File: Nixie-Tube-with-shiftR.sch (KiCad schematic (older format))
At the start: 56 parts, among them J1 Conn_01x06_Male, J2 HV_IN, J3 Conn_01x06_Female, J4 HV_OUT, Q1 MMBTA42LT1, Q10 MMBTA42LT1, Q11 AO3400, Q12 AO3400, Q13 AO3400, Q14 MMBTA42LT1, Q15 MMBTA42LT1, Q2 MMBTA42LT1, Q3 MMBTA42LT1, Q4 MMBTA42LT1, Q5 MMBTA42LT1, Q6 MMBTA42LT1, Q7 MMBTA42LT1, Q8 MMBTA42LT1, Q9 MMBTA42LT1, U1 74HC595D, U2 nixie-tube, U3 74HC595D, U4 ams1117-5.0

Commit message: rename file according to the project
nixie-tube-display-with-shiftR is qs27 while roundxx is qs30
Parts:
- removed U2: nixie-tube, symbol nixie-tube
- added U?: nixie-tube-qs27, symbol nixie-tube-qs27
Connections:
- no-connect marks 3 -> 1
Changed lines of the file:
@@
 $EndComp
 $Comp
-L nixie-tube U2
-U 1 1 5A0CB7BC
+L nixie-tube-qs27 U?
+U 1 1 5A0CF6F4
 P 5450 1950
-F 0 "U2" H 4875 2050 60  0000 C CNN
-F 1 "nixie-tube" H 5625 2275 60  0000 C CNN
+F 0 "U?" H 4875 2050 60  0000 C CNN
+F 1 "nixie-tube-qs27" H 5625 2275 60  0000 C CNN
 F 2 "" H 5150 1975 60  0001 C CNN
 F 3 "" H 5150 1975 60  0001 C CNN
@@
 	1    0    0    -1
 $EndComp
-NoConn ~ 5025 1325
-NoConn ~ 5150 1325
 $EndSCHEMATC

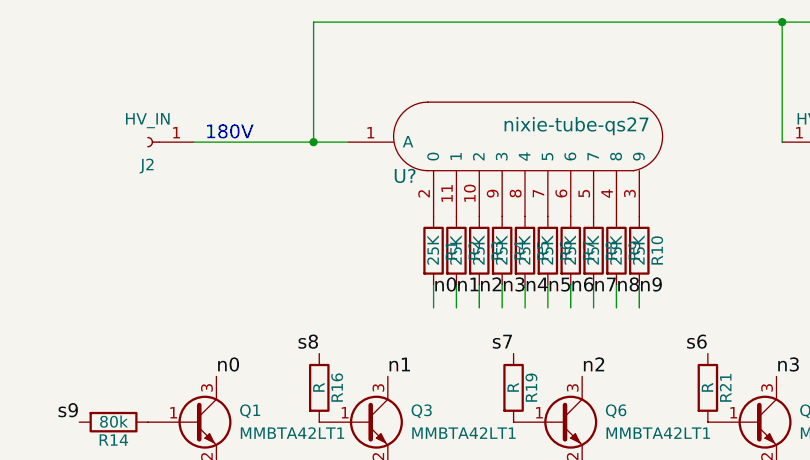
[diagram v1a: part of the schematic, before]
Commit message: remove silkscreen on female pins, re routed some of the tracks
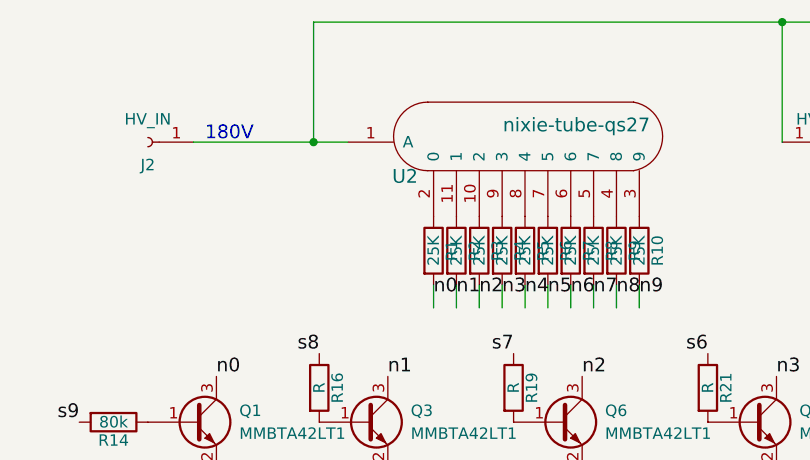
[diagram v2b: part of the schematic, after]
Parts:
- J2: footprint Socket_Strips:Socket_Strip_Angled_1x01_Pitch2.54mm -> nixie-tube-fp:Socket_Strip_Angled_1x01_Pitch2.54mm_without_silk
- J3: footprint Socket_Strips:Socket_Strip_Angled_1x06_Pitch2.54mm -> nixie-tube-fp:Socket_Strip_Angled_1x06_Pitch2.54mm_without_silk
- gave numbers to parts that had none: 1
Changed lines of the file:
@@
 F 0 "J2" H 3750 1800 50  0000 C CNN
 F 1 "HV_IN" H 3750 1600 50  0000 C CNN
-F 2 "Socket_Strips:Socket_Strip_Angled_1x01_Pitch2.54mm" H 3750 1700 50  0001 C CNN
+F 2 "nixie-tube-fp:Socket_Strip_Angled_1x01_Pitch2.54mm_without_silk" H 3750 1700 50  0001 C CNN
 F 3 "" H 3750 1700 50  0001 C CNN
 	1    3750 1700
@@
 F 0 "J3" H 3525 4150 50  0000 C CNN
 F 1 "Conn_01x06_Female" H 3525 3450 50  0000 C CNN
-F 2 "Socket_Strips:Socket_Strip_Angled_1x06_Pitch2.54mm" H 3525 3850 50  0001 C CNN
+F 2 "nixie-tube-fp:Socket_Strip_Angled_1x06_Pitch2.54mm_without_silk" H 3525 3850 50  0001 C CNN
 F 3 "" H 3525 3850 50  0001 C CNN
 	1    3525 3850
@@
 $EndComp
 $Comp
-L nixie-tube-qs27 U?
+L nixie-tube-qs27 U2
 U 1 1 5A0CF6F4
 P 5450 1950
-F 0 "U?" H 4875 2050 60  0000 C CNN
+F 0 "U2" H 4875 2050 60  0000 C CNN
 F 1 "nixie-tube-qs27" H 5625 2275 60  0000 C CNN
 F 2 "" H 5150 1975 60  0001 C CNN

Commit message: fixed various bugs
RGB led not connected properly to the mosfet
AO3400 pin orientation is not same with datasheet
move silkscreen away on neon footprint
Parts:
- removed D1: LED_CRGB, nixie-tube-fp:Rgb-Led, symbol LED_CRGB
- removed Q11, Q12, Q13: AO3400, TO_SOT_Packages_SMD:SOT-23, symbol 2N7000
- added D1: LED_RGB_BGR, nixie-tube-fp:LED_RGB_5050-6, symbol LED_RGB_BGR
- added Q11, Q12, Q13: AO3400, TO_SOT_Packages_SMD:SOT-23, symbol 2N7002
- U2: footprint (none) -> nixie-tube-fp:qs27-1
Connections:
- wire segments 66 -> 68
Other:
- moved on the sheet: R11, R12, R13
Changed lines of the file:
@@
 	6525 5700 6525 5725
 NoConn ~ 6325 4250
-$Comp
-L LED_CRGB D1
-U 1 1 59DF14B9
-P 8375 5750
-F 0 "D1" H 8375 6120 50  0000 C CNN
-F 1 "LED_CRGB" H 8375 5400 50  0000 C CNN
-F 2 "nixie-tube-fp:Rgb-Led" H 8375 5700 50  0001 C CNN
-F 3 "" H 8375 5700 50  0001 C CNN
-	1    8375 5750
-	0    -1   -1   0
-$EndComp
-$Comp
-L GND #PWR05
-U 1 1 59DF166A
-P 8375 5950
-F 0 "#PWR05" H 8375 5700 50  0001 C CNN
-F 1 "GND" H 8375 5800 50  0000 C CNN
-F 2 "" H 8375 5950 50  0001 C CNN
-F 3 "" H 8375 5950 50  0001 C CNN
-	1    8375 5950
-	1    0    0    -1
-$EndComp
 Text Label 7725 5150 2    60   ~ 0
 Red
-Text Label 8625 5175 2    60   ~ 0
+Text Label 8625 5150 2    60   ~ 0
 Green
-Text Label 9400 5175 2    60   ~ 0
+Text Label 9400 5150 2    60   ~ 0
 Blue
 Text Label 5825 4250 1    60   ~ 0
@@
 Blue
 Wire Wire Line
-	8025 5350 8025 5550
-Wire Wire Line
-	8025 5550 8175 5550
-Wire Wire Line
-	8925 5375 8375 5375
-Wire Wire Line
-	8375 5375 8375 5550
-Wire Wire Line
-	9700 5375 9700 5550
-Wire Wire Line
-	9700 5550 8575 5550
-Wire Wire Line
 	3950 1700 4625 1700
 $Comp
 L R R11
 U 1 1 59DF3F26
-P 8025 4800
-F 0 "R11" V 8105 4800 50  0000 C CNN
-F 1 "500" V 8025 4800 50  0000 C CNN
-F 2 "Resistors_SMD:R_0603" V 7955 4800 50  0001 C CNN
-F 3 "" H 8025 4800 50  0001 C CNN
-	1    8025 4800
+P 8075 4025
+F 0 "R11" V 8155 4025 50  0000 C CNN
+F 1 "500" V 8075 4025 50  0000 C CNN
+F 2 "Resistors_SMD:R_0603" V 8005 4025 50  0001 C CNN
+F 3 "" H 8075 4025 50  0001 C CNN
+	1    8075 4025
 	1    0    0    -1
 $EndComp
@@
 L R R12
 U 1 1 59DF4051
-P 8925 4825
-F 0 "R12" V 9005 4825 50  0000 C CNN
-F 1 "500" V 8925 4825 50  0000 C CNN
-F 2 "Resistors_SMD:R_0603" V 8855 4825 50  0001 C CNN
-F 3 "" H 8925 4825 50  0001 C CNN
-	1    8925 4825
+P 8275 4025
+F 0 "R12" V 8355 4025 50  0000 C CNN
+F 1 "500" V 8275 4025 50  0000 C CNN
+F 2 "Resistors_SMD:R_0603" V 8205 4025 50  0001 C CNN
+F 3 "" H 8275 4025 50  0001 C CNN
+	1    8275 4025
 	1    0    0    -1
 $EndComp
@@
 L R R13
 U 1 1 59DF4103
-P 9700 4825
-F 0 "R13" V 9780 4825 50  0000 C CNN
-F 1 "500" V 9700 4825 50  0000 C CNN
-F 2 "Resistors_SMD:R_0603" V 9630 4825 50  0001 C CNN
-F 3 "" H 9700 4825 50  0001 C CNN
-	1    9700 4825
+P 8475 4025
+F 0 "R13" V 8555 4025 50  0000 C CNN
+F 1 "500" V 8475 4025 50  0000 C CNN
+F 2 "Resistors_SMD:R_0603" V 8405 4025 50  0001 C CNN
+F 3 "" H 8475 4025 50  0001 C CNN
+	1    8475 4025
 	1    0    0    -1
 $EndComp
@@
 DotU
 $Comp
-L GND #PWR06
+L GND #PWR05
 U 1 1 59E03A8E
 P 7775 2350
-F 0 "#PWR06" H 7775 2100 50  0001 C CNN
+F 0 "#PWR05" H 7775 2100 50  0001 C CNN
 F 1 "GND" H 7775 2200 50  0000 C CNN
 F 2 "" H 7775 2350 50  0001 C CNN
@@
 	5225 5925 5225 5625
 $Comp
-L GND #PWR07
+L GND #PWR06
 U 1 1 59E07C89
 P 2800 3525
-F 0 "#PWR07" H 2800 3275 50  0001 C CNN
+F 0 "#PWR06" H 2800 3275 50  0001 C CNN
 F 1 "GND" H 2800 3375 50  0000 C CNN
 F 2 "" H 2800 3525 50  0001 C CNN
@@
 	1525 5375 1700 5375
 $Comp
-L +5V #PWR08
+L +5V #PWR07
 U 1 1 59E0CEE2
 P 3000 5300
-F 0 "#PWR08" H 3000 5150 50  0001 C CNN
+F 0 "#PWR07" H 3000 5150 50  0001 C CNN
 F 1 "+5V" H 3000 5440 50  0000 C CNN
 F 2 "" H 3000 5300 50  0001 C CNN
@@
 	3000 5375 3000 5300
 $Comp
-L GND #PWR09
+L GND #PWR08
 U 1 1 59E0CFCB
 P 2200 5975
-F 0 "#PWR09" H 2200 5725 50  0001 C CNN
+F 0 "#PWR08" H 2200 5725 50  0001 C CNN
 F 1 "GND" H 2200 5825 50  0000 C CNN
 F 2 "" H 2200 5975 50  0001 C CNN
@@
 	2200 5825 2200 5975
 $Comp
-L +5V #PWR010
+L +5V #PWR09
 U 1 1 59E0E450
 P 3700 5675
-F 0 "#PWR010" H 3700 5525 50  0001 C CNN
+F 0 "#PWR09" H 3700 5525 50  0001 C CNN
 F 1 "+5V" H 3700 5815 50  0000 C CNN
 F 2 "" H 3700 5675 50  0001 C CNN
@@
 $EndComp
 $Comp
-L +5V #PWR011
+L +5V #PWR010
 U 1 1 59E0E605
 P 4700 5850
-F 0 "#PWR011" H 4700 5700 50  0001 C CNN
+F 0 "#PWR010" H 4700 5700 50  0001 C CNN
 F 1 "+5V" H 4700 5990 50  0000 C CNN
 F 2 "" H 4700 5850 50  0001 C CNN
@@
 $EndComp
 $Comp
-L +5V #PWR012
+L +5V #PWR011
 U 1 1 59E0EA7E
 P 5225 5625
-F 0 "#PWR012" H 5225 5475 50  0001 C CNN
+F 0 "#PWR011" H 5225 5475 50  0001 C CNN
 F 1 "+5V" H 5225 5765 50  0000 C CNN
 F 2 "" H 5225 5625 50  0001 C CNN
@@
 $EndComp
 $Comp
-L +5V #PWR013
+L +5V #PWR012
 U 1 1 59E0EB56
 P 6325 5725
-F 0 "#PWR013" H 6325 5575 50  0001 C CNN
+F 0 "#PWR012" H 6325 5575 50  0001 C CNN
 F 1 "+5V" H 6325 5865 50  0000 C CNN
 F 2 "" H 6325 5725 50  0001 C CNN
@@
 DotD
 $Comp
-L GND #PWR014
+L GND #PWR013
 U 1 1 59E1EE92
 P 8725 2350
-F 0 "#PWR014" H 8725 2100 50  0001 C CNN
+F 0 "#PWR013" H 8725 2100 50  0001 C CNN
 F 1 "GND" H 8725 2200 50  0000 C CNN
 F 2 "" H 8725 2350 50  0001 C CNN
@@
 	2050 3650 3325 3650
 $Comp
+L +5V #PWR014
+U 1 1 59EE23C2
+P 8075 3875
+F 0 "#PWR014" H 8075 3725 50  0001 C CNN
+F 1 "+5V" H 8075 4015 50  0000 C CNN
+F 2 "" H 8075 3875 50  0001 C CNN
+F 3 "" H 8075 3875 50  0001 C CNN
+	1    8075 3875
+	1    0    0    -1
+$EndComp
+$Comp
 L +5V #PWR015
-U 1 1 59EE23C2
-P 8025 4650
-F 0 "#PWR015" H 8025 4500 50  0001 C CNN
-F 1 "+5V" H 8025 4790 50  0000 C CNN
-F 2 "" H 8025 4650 50  0001 C CNN
-F 3 "" H 8025 4650 50  0001 C CNN
-	1    8025 4650
+U 1 1 59EE25D6
+P 8275 3875
+F 0 "#PWR015" H 8275 3725 50  0001 C CNN
+F 1 "+5V" H 8275 4015 50  0000 C CNN
+F 2 "" H 8275 3875 50  0001 C CNN
+F 3 "" H 8275 3875 50  0001 C CNN
+	1    8275 3875
 	1    0    0    -1
 $EndComp
 $Comp
 L +5V #PWR016
-U 1 1 59EE25D6
-P 8925 4675
-F 0 "#PWR016" H 8925 4525 50  0001 C CNN
-F 1 "+5V" H 8925 4815 50  0000 C CNN
-F 2 "" H 8925 4675 50  0001 C CNN
-F 3 "" H 8925 4675 50  0001 C CNN
-	1    8925 4675
-	1    0    0    -1
-$EndComp
-$Comp
-L +5V #PWR017
 U 1 1 59EE2686
-P 9700 4675
-F 0 "#PWR017" H 9700 4525 50  0001 C CNN
-F 1 "+5V" H 9700 4815 50  0000 C CNN
-F 2 "" H 9700 4675 50  0001 C CNN
-F 3 "" H 9700 4675 50  0001 C CNN
-	1    9700 4675
+P 8475 3875
+F 0 "#PWR016" H 8475 3725 50  0001 C CNN
+F 1 "+5V" H 8475 4015 50  0000 C CNN
+F 2 "" H 8475 3875 50  0001 C CNN
+F 3 "" H 8475 3875 50  0001 C CNN
+	1    8475 3875
 	1    0    0    -1
 $EndComp
@@
 STORE
 $Comp
-L +VDC #PWR018
+L +VDC #PWR017
 U 1 1 5A0A5D8C
 P 2575 3175
-F 0 "#PWR018" H 2575 3075 50  0001 C CNN
+F 0 "#PWR017" H 2575 3075 50  0001 C CNN
 F 1 "+VDC" H 2575 3425 50  0000 C CNN
 F 2 "" H 2575 3175 50  0001 C CNN
@@
 $EndComp
 $Comp
-L +VDC #PWR019
+L +VDC #PWR018
 U 1 1 5A0A64FC
 P 1525 5175
-F 0 "#PWR019" H 1525 5075 50  0001 C CNN
+F 0 "#PWR018" H 1525 5075 50  0001 C CNN
 F 1 "+VDC" H 1525 5425 50  0000 C CNN
 F 2 "" H 1525 5175 50  0001 C CNN
@@
 STORE
 $Comp
-L GND #PWR020
+L GND #PWR019
 U 1 1 5A0B1CC9
 P 4600 5675
-F 0 "#PWR020" H 4600 5425 50  0001 C CNN
+F 0 "#PWR019" H 4600 5425 50  0001 C CNN
 F 1 "GND" H 4600 5525 50  0000 C CNN
 F 2 "" H 4600 5675 50  0001 C CNN
@@
 $EndComp
 $Comp
-L GND #PWR021
+L GND #PWR020
 U 1 1 5A0B2485
 P 6225 5650
-F 0 "#PWR021" H 6225 5400 50  0001 C CNN
+F 0 "#PWR020" H 6225 5400 50  0001 C CNN
 F 1 "GND" H 6225 5500 50  0000 C CNN
 F 2 "" H 6225 5650 50  0001 C CNN
@@
 $EndComp
 $Comp
-L 2N7000 Q11
-U 1 1 5A0C81E8
+L nixie-tube-qs27 U2
+U 1 1 5A0CF6F4
+P 5450 1950
+F 0 "U2" H 4875 2050 60  0000 C CNN
+F 1 "nixie-tube-qs27" H 5625 2275 60  0000 C CNN
+F 2 "nixie-tube-fp:qs27-1" H 5150 1975 60  0001 C CNN
+F 3 "" H 5150 1975 60  0001 C CNN
+	1    5450 1950
+	1    0    0    -1
+$EndComp
+Wire Wire Line
+	8025 4950 8025 4575
+Wire Wire Line
+	8025 4575 8075 4575
+Wire Wire Line
+	8475 4575 9700 4575
+Wire Wire Line
+	8275 4575 8275 4950
+Wire Wire Line
+	8025 5350 9700 5350
+Wire Wire Line
+	9700 4575 9700 4950
+Connection ~ 8925 5350
+Wire Wire Line
+	8925 5350 8925 5425
+$Comp
+L GND #PWR021
+U 1 1 5A101848
+P 8925 5425
+F 0 "#PWR021" H 8925 5175 50  0001 C CNN
+F 1 "GND" H 8925 5275 50  0000 C CNN
+F 2 "" H 8925 5425 50  0001 C CNN
+F 3 "" H 8925 5425 50  0001 C CNN
+	1    8925 5425
+	1    0    0    -1
+$EndComp
+$Comp
+L LED_RGB_BGR D1
+U 1 1 5A100DCA
+P 8275 4375
+F 0 "D1" H 8275 4745 50  0000 C CNN
+F 1 "LED_RGB_BGR" H 8275 4025 50  0000 C CNN
+F 2 "nixie-tube-fp:LED_RGB_5050-6" H 8275 4325 50  0001 C CNN
+F 3 "" H 8275 4325 50  0001 C CNN
+	1    8275 4375
+	0    -1   -1   0
+$EndComp
+$Comp
+L 2N7002 Q11
+U 1 1 5A10300F
 P 7925 5150
 F 0 "Q11" H 8125 5225 50  0000 L CNN
@@
 $EndComp
 $Comp
-L 2N7000 Q12
-U 1 1 5A0C89DD
-P 8825 5175
-F 0 "Q12" H 9025 5250 50  0000 L CNN
-F 1 "AO3400" H 9025 5175 50  0000 L CNN
-F 2 "TO_SOT_Packages_SMD:SOT-23" H 9025 5100 50  0001 L CIN
-F 3 "" H 8825 5175 50  0001 L CNN
-	1    8825 5175
-	1    0    0    -1
-$EndComp
-$Comp
-L 2N7000 Q13
-U 1 1 5A0C8AB1
-P 9600 5175
-F 0 "Q13" H 9800 5250 50  0000 L CNN
-F 1 "AO3400" H 9800 5175 50  0000 L CNN
-F 2 "TO_SOT_Packages_SMD:SOT-23" H 9800 5100 50  0001 L CIN
-F 3 "" H 9600 5175 50  0001 L CNN
-	1    9600 5175
-	1    0    0    -1
-$EndComp
-$Comp
-L nixie-tube-qs27 U2
-U 1 1 5A0CF6F4
-P 5450 1950
-F 0 "U2" H 4875 2050 60  0000 C CNN
-F 1 "nixie-tube-qs27" H 5625 2275 60  0000 C CNN
-F 2 "" H 5150 1975 60  0001 C CNN
-F 3 "" H 5150 1975 60  0001 C CNN
-	1    5450 1950
-	1    0    0    -1
-$EndComp
+L 2N7002 Q12
+U 1 1 5A1035D4
+P 8825 5150
+F 0 "Q12" H 9025 5225 50  0000 L CNN
+F 1 "AO3400" H 9025 5150 50  0000 L CNN
+F 2 "TO_SOT_Packages_SMD:SOT-23" H 9025 5075 50  0001 L CIN
+F 3 "" H 8825 5150 50  0001 L CNN
+	1    8825 5150
+	1    0    0    -1
+$EndComp
+$Comp
+L 2N7002 Q13
+U 1 1 5A104F72
+P 9600 5150
+F 0 "Q13" H 9800 5225 50  0000 L CNN
+F 1 "AO3400" H 9800 5150 50  0000 L CNN
+F 2 "TO_SOT_Packages_SMD:SOT-23" H 9800 5075 50  0001 L CIN
+F 3 "" H 9600 5150 50  0001 L CNN
+	1    9600 5150
+	1    0    0    -1
+$EndComp
+Wire Wire Line
+	8275 4950 8925 4950
 $EndSCHEMATC

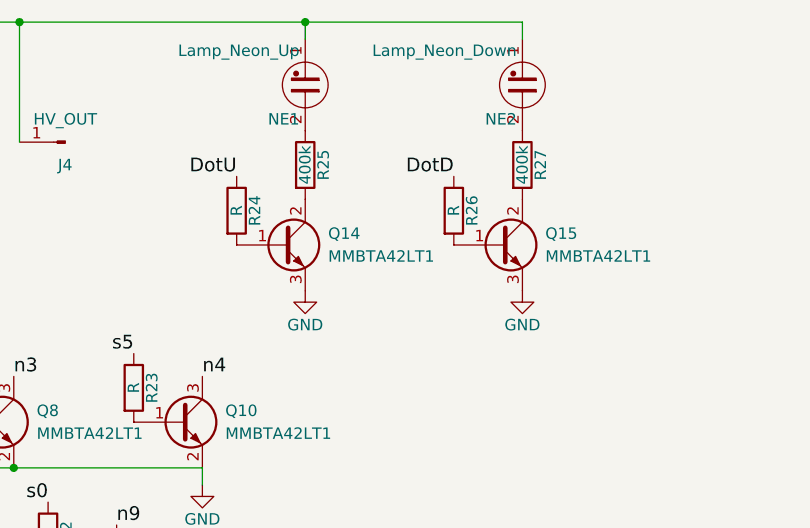
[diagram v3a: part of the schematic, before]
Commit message: fixed 2 of the mmbta42 transistor pin number errors
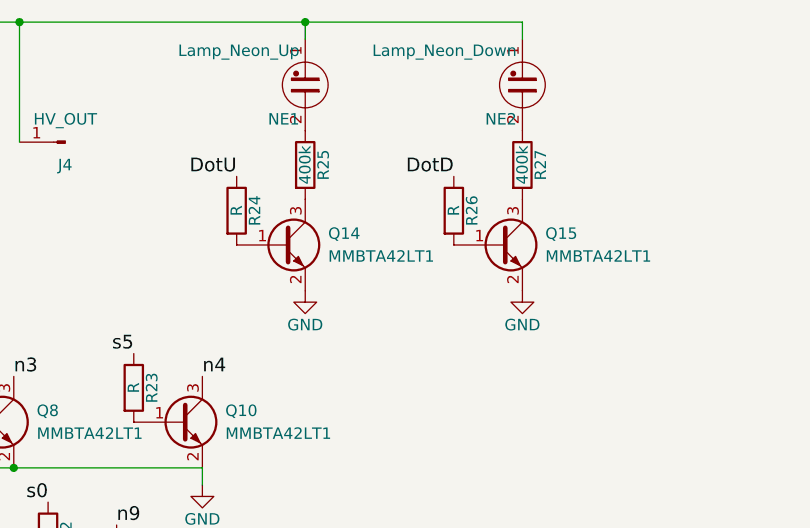
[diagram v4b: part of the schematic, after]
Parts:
- removed Q14, Q15: MMBTA42LT1, TO_SOT_Packages_SMD:SOT-23, symbol Q_NPN_BCE
- added Q14, Q15: MMBTA42LT1, TO_SOT_Packages_SMD:SOT-23, symbol Q_NPN_BEC
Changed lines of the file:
@@
 MOSI-OUT
-$Comp
-L Q_NPN_BCE Q14
-U 1 1 59E02747
-P 7675 2150
-F 0 "Q14" H 7875 2200 50  0000 L CNN
-F 1 "MMBTA42LT1" H 7875 2100 50  0000 L CNN
-F 2 "TO_SOT_Packages_SMD:SOT-23" H 7875 2250 50  0001 C CNN
-F 3 "" H 7675 2150 50  0001 C CNN
-	1    7675 2150
-	1    0    0    -1
-$EndComp
 $Comp
 L R R24
@@
 Connection ~ 6525 1175
 $Comp
-L Q_NPN_BCE Q15
-U 1 1 59E1EE85
-P 8625 2150
-F 0 "Q15" H 8825 2200 50  0000 L CNN
-F 1 "MMBTA42LT1" H 8825 2100 50  0000 L CNN
-F 2 "TO_SOT_Packages_SMD:SOT-23" H 8825 2250 50  0001 C CNN
-F 3 "" H 8625 2150 50  0001 C CNN
-	1    8625 2150
-	1    0    0    -1
-$EndComp
-$Comp
 L R R26
 U 1 1 59E1EE8B
@@
 Wire Wire Line
 	8275 4950 8925 4950
+$Comp
+L Q_NPN_BEC Q14
+U 1 1 5A112411
+P 7675 2150
+F 0 "Q14" H 7875 2200 50  0000 L CNN
+F 1 "MMBTA42LT1" H 7875 2100 50  0000 L CNN
+F 2 "TO_SOT_Packages_SMD:SOT-23" H 7875 2250 50  0001 C CNN
+F 3 "" H 7675 2150 50  0001 C CNN
+	1    7675 2150
+	1    0    0    -1
+$EndComp
+$Comp
+L Q_NPN_BEC Q15
+U 1 1 5A1124E6
+P 8625 2150
+F 0 "Q15" H 8825 2200 50  0000 L CNN
+F 1 "MMBTA42LT1" H 8825 2100 50  0000 L CNN
+F 2 "TO_SOT_Packages_SMD:SOT-23" H 8825 2250 50  0001 C CNN
+F 3 "" H 8625 2150 50  0001 C CNN
+	1    8625 2150
+	1    0    0    -1
+$EndComp
 $EndSCHEMATC

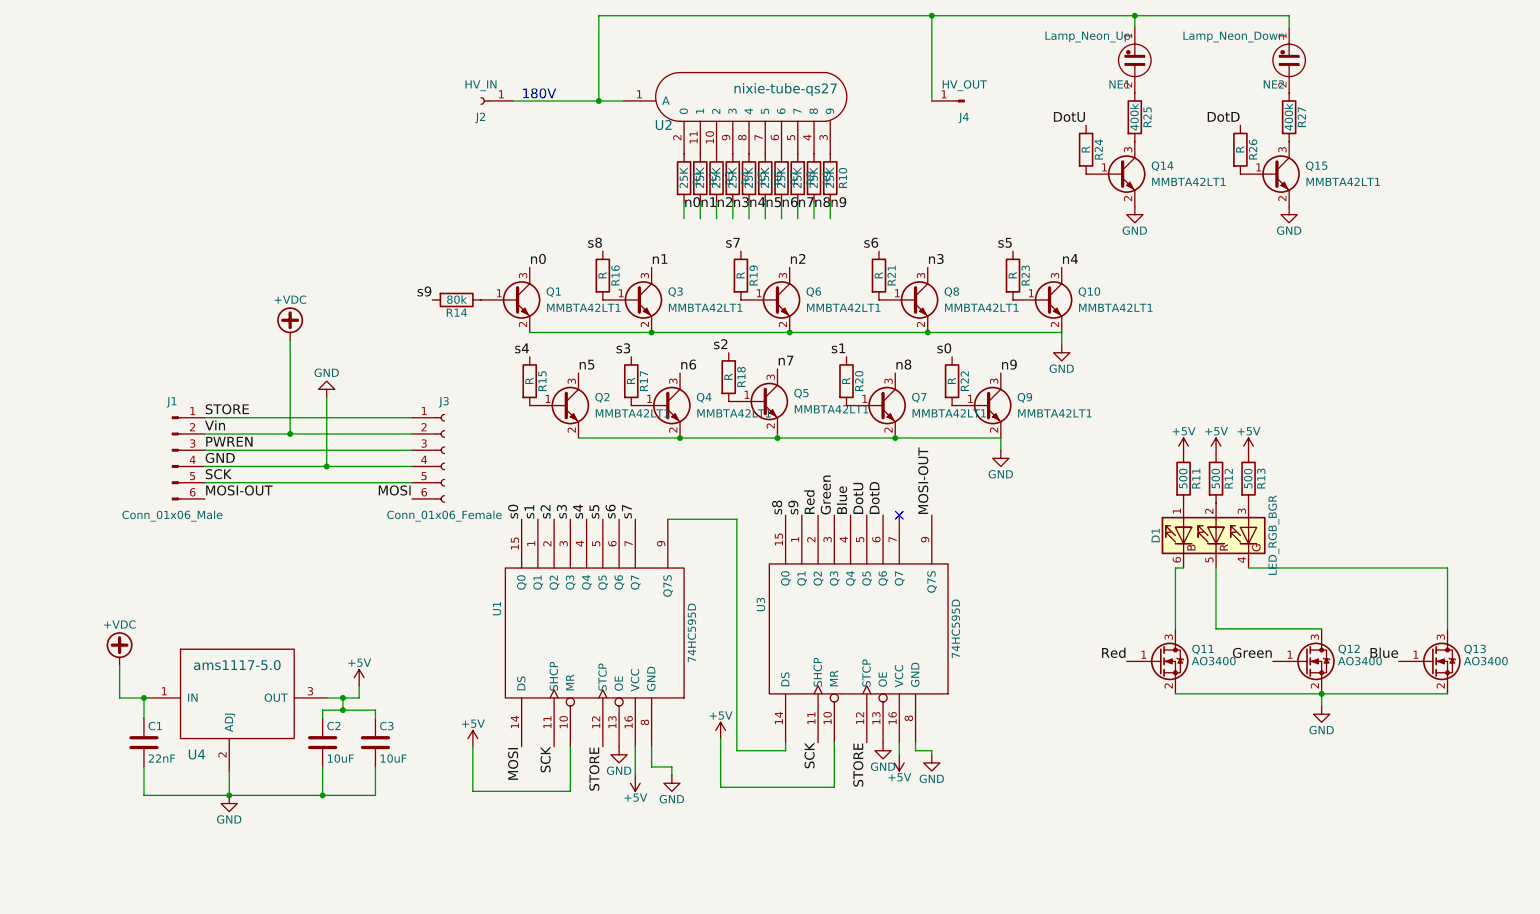
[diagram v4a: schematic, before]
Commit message: nixie's legs pin assignment needs to be change
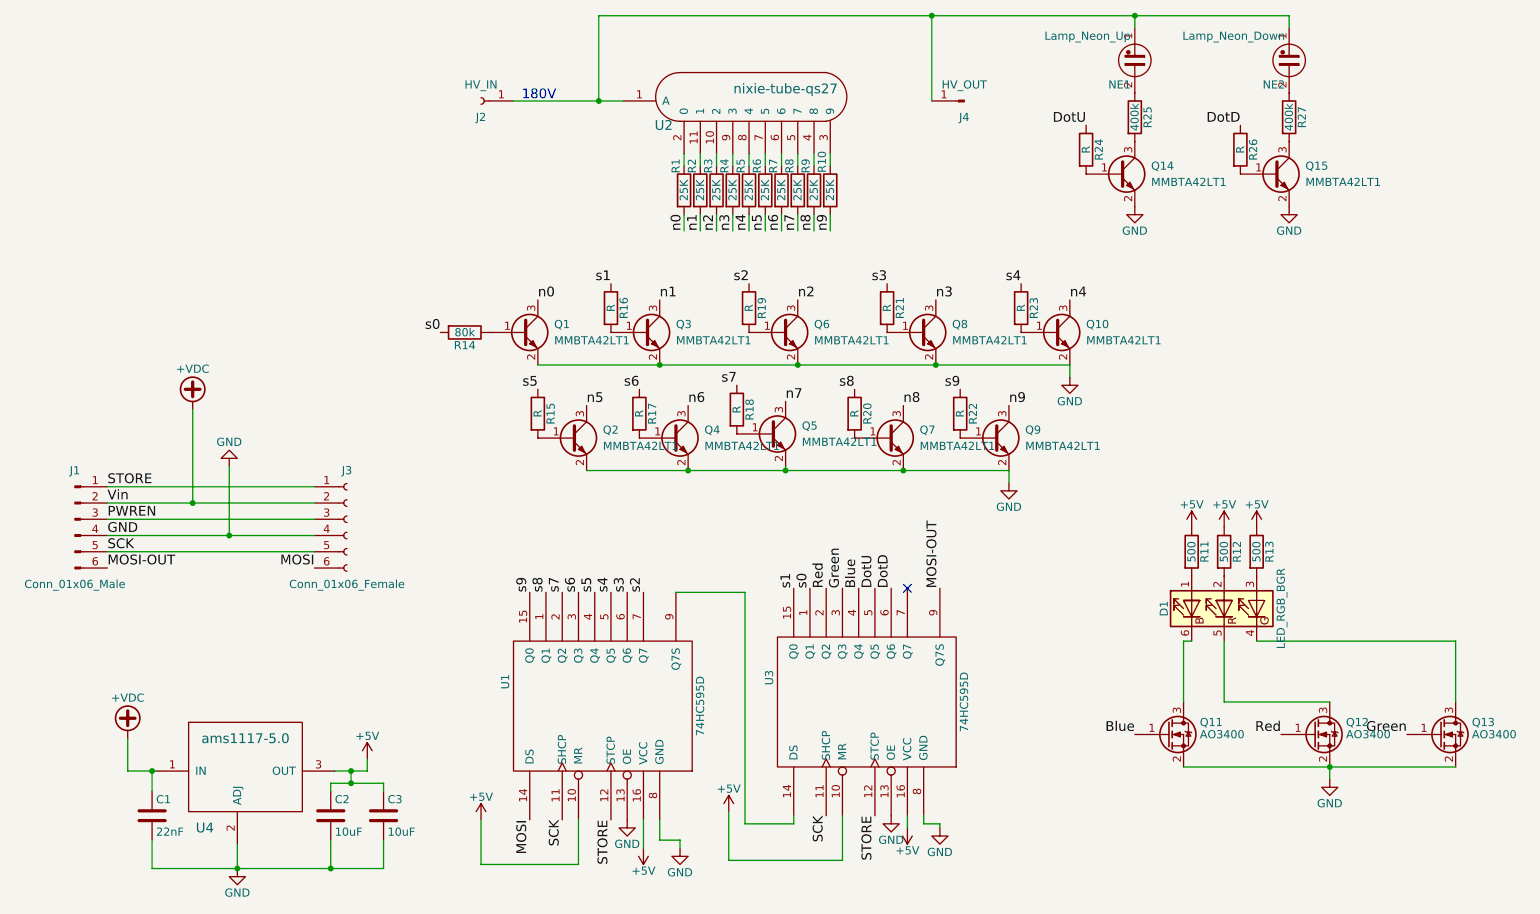
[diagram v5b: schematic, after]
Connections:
- wire segments 68 -> 78
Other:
- moved on the sheet: C1, C2, C3, D1, J1, J3, Q1, Q10, Q11, Q12, Q13, Q2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
